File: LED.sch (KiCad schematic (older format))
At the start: 24 parts, among them U1 74LS595, U2 74LS595

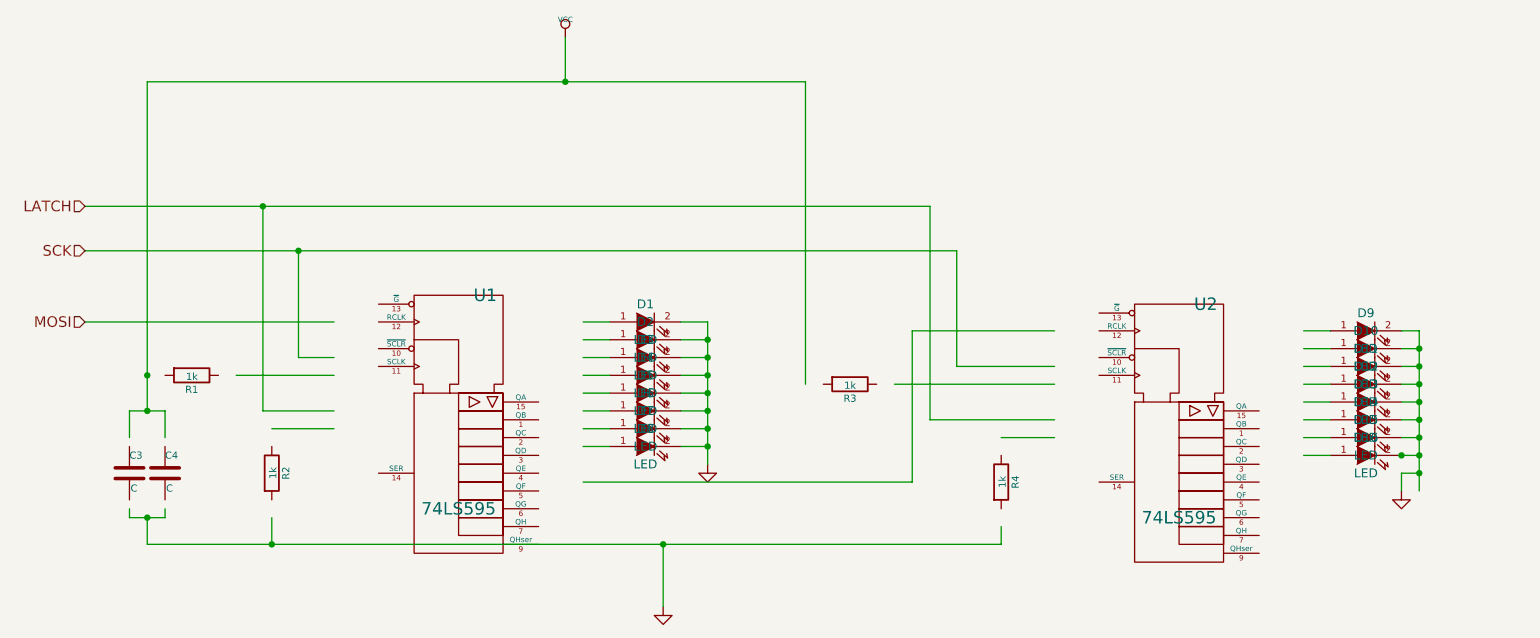
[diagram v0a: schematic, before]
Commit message: Added MAX7219 and LEDs
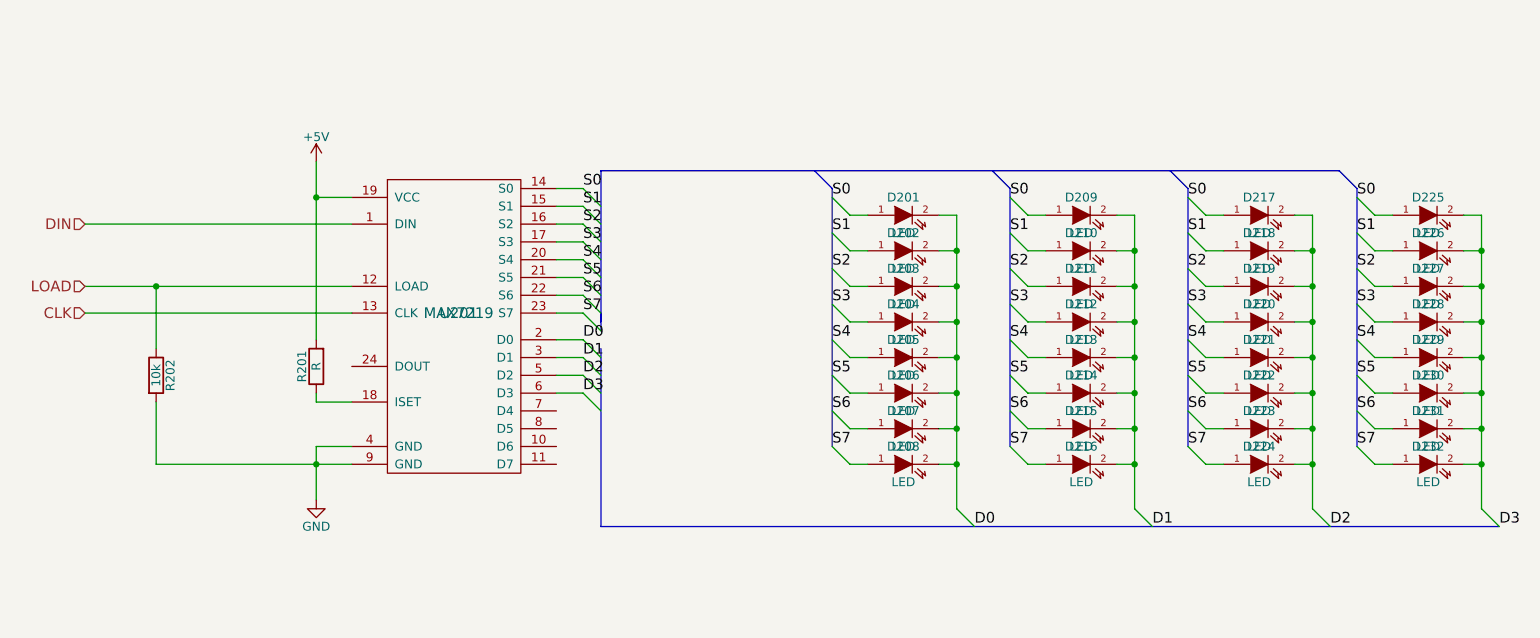
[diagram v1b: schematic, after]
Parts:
- removed C3, C4: C, symbol C
- removed D1, D10, D11, D12, D13, D14, D15, D16, D2, D3, D4, D5, D6, D7, D8, D9: LED, symbol LED
- removed R1, R2, R3, R4: 1k, symbol R
- removed U1, U2: 74LS595, symbol 74LS595
- added D201, D202, D203, D204, D205, D206, D207, D208, D209, D210, D211, D212, D213, D214, D215, D216, D217, D218, D219, D220, D221, D222, D223, D224, D225, D226, D227, D228, D229, D230, D231, D232: LED, symbol LED
- added R201: R, symbol R
- added R202: 10k, symbol R
- added U201: MAX7219, symbol MAX7219
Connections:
- net labels added: +5V, CLK, D0, D1, D2, D3, DIN, LOAD, S0, S1, S2, S3, S4, S5, S6, S7
- net labels removed: LATCH, MOSI, SCK, VCC
- wire segments 69 -> 92
